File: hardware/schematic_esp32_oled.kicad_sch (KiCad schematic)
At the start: 21 parts, among them J1 AUDIO_JACK_2.5MMSPECIAL_POGO_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, U1 SI4735-D60-GU, U2 ESP32-DEVKITC-32D, Y1 CRYSTALPTH-2X6

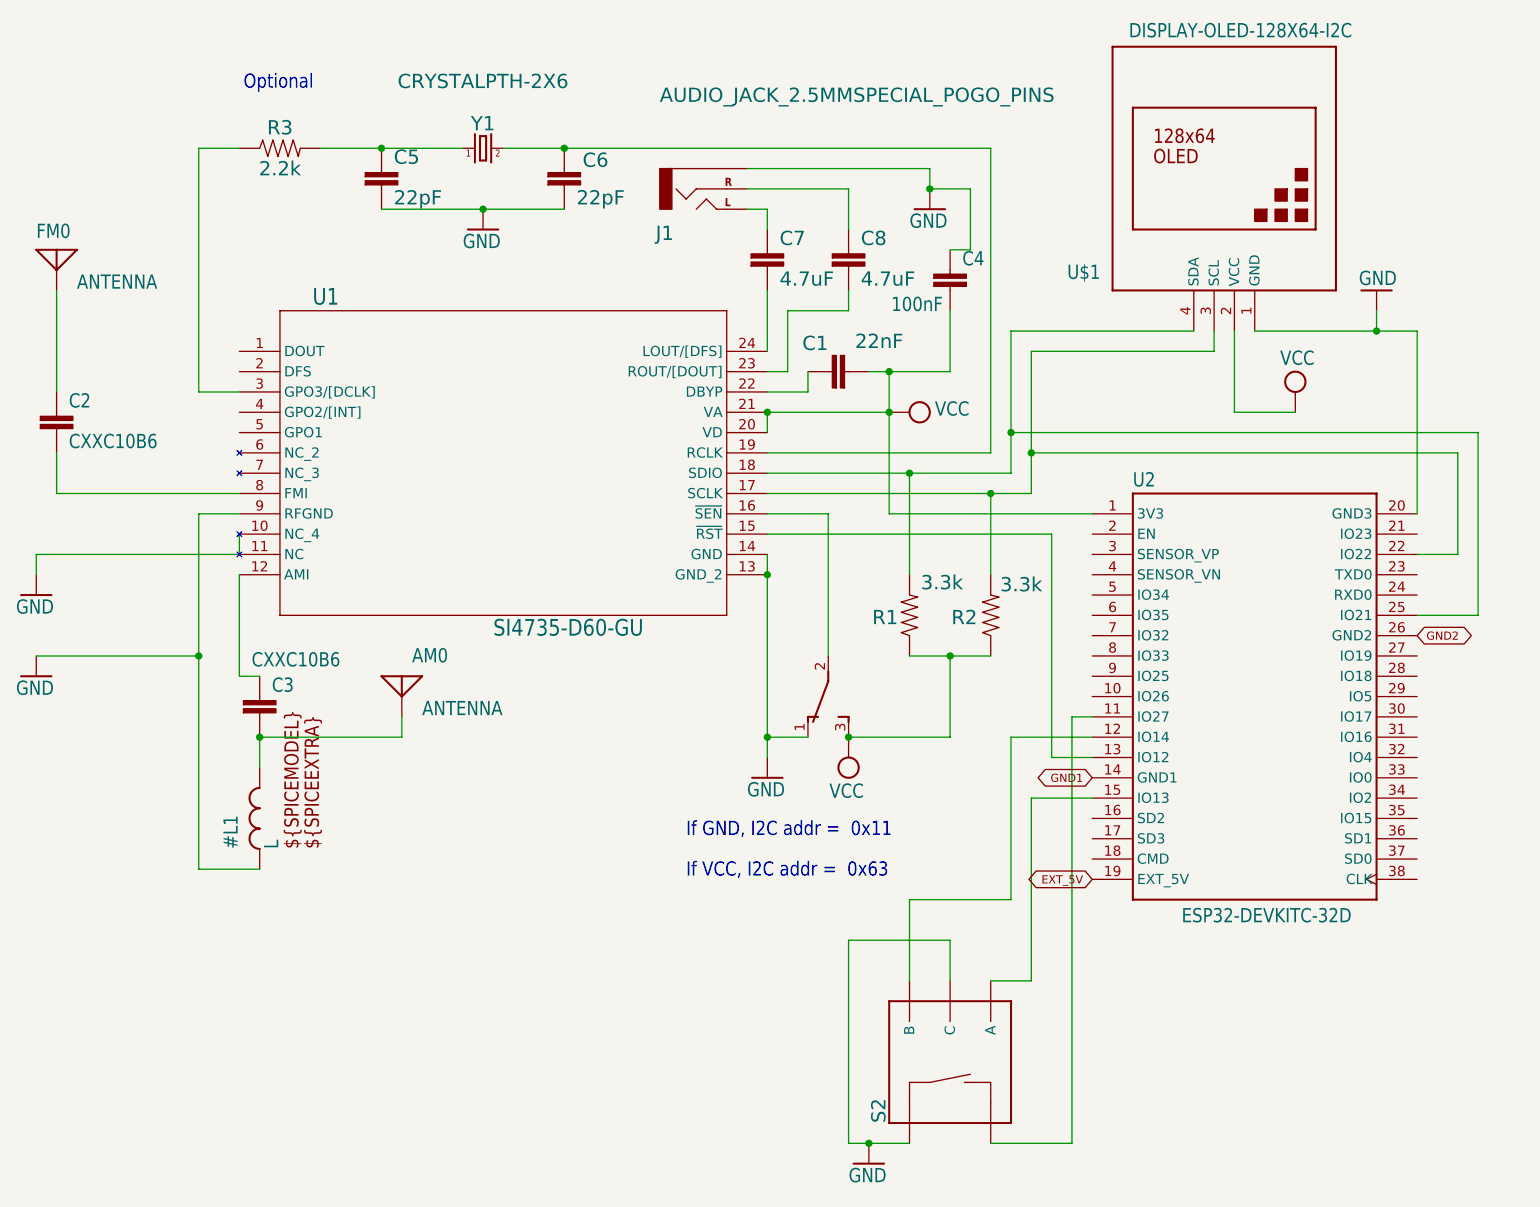
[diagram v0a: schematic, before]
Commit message: new file:   hardware/Datasheet/Si4730-31-34-35-D60.pdf 	new file:   hardware/schematic_esp32_oled-backups/schematic_esp32_oled-2025-01-23_103532.zip 	modified:   hardware/schematic_esp32_oled.kicad_sch
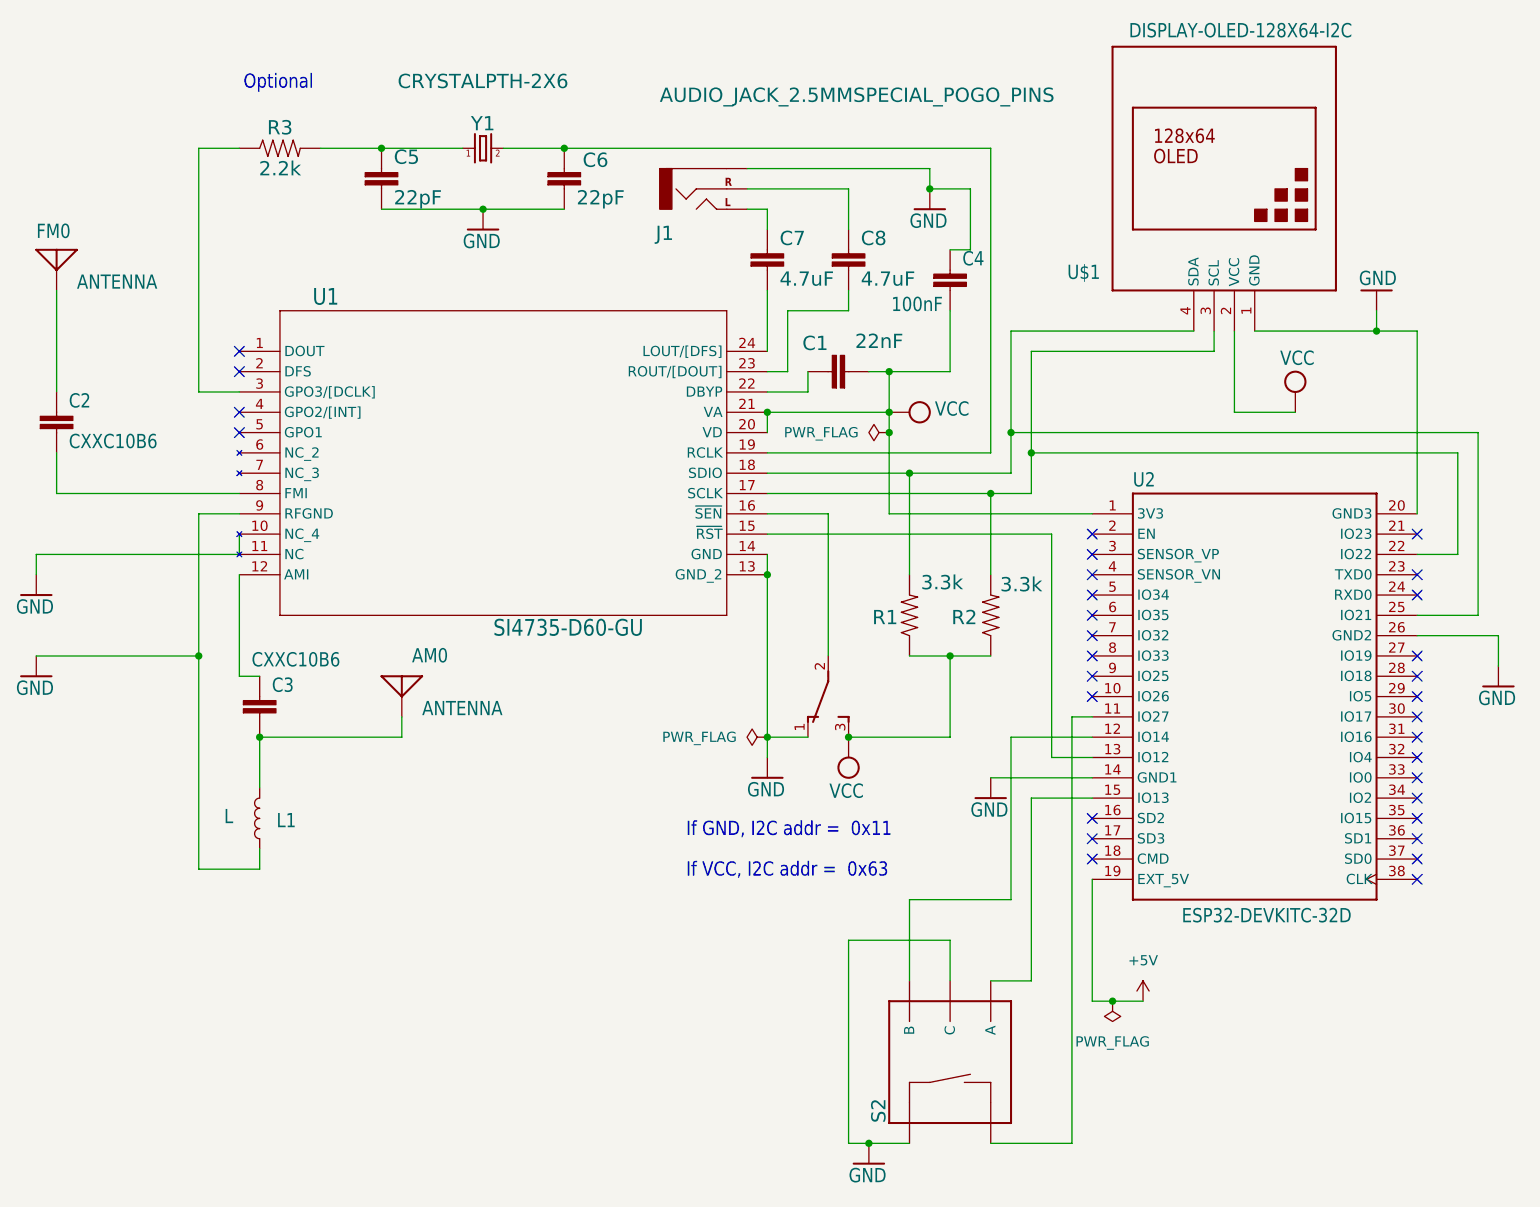
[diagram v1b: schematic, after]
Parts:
- L1: renamed from #L1; symbol schematic_esp32_oled-eagle-import:L -> Device:L
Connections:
- net GND1 is gone; now on net GND: U2.14 (GND1)
- net GND2 is gone; now on net GND: U2.26 (GND2)
- net EXT_5V renamed +5V
- no-connect marks 0 -> 31
